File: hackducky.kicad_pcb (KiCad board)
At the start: 2 copper layers, 21 x 42.4 mm, 52 parts, among them J1 USB_A, J2 Conn_02x02_Top_Bottom, J3 Micro_SD_Card, P2 USB_C_Plug, SW3 BOOT_SEL, SW4 BOOT_SEL, U1 W25Q16JVSS, U2 AP2112K-3.3, U3 USBLC6-2P6, U4 RP2040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

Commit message: done beter
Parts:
- moved G*** 1.85 mm to (82.5, 86.6)
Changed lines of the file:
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@@
 	(footprint "LOGO"
 		(layer "F.Cu")
-		(at 82.5 84.75 90)
+		(at 82.45 86.6 90)
 		(property "Reference" "G***"
 			(at 0 0 90)
@@
 	)
 	(gr_text "Souptik.me & Aarav J."
-		(at 90.5 93 -90)
+		(at 93.68 92.44 -90)
 		(layer "F.SilkS")
 		(effects

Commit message: will do pr latr
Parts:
- R16, R17, R18, R19, R20, R21: moved to B.Cu
- moved G*** 3.71 mm to (91.9, 87.9)
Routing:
- net +3V3: track 103.6 -> 113.2 mm, vias 9 -> 12
- net GND: track 94.1 -> 101.2 mm
- net SD_CLK: track 21.2 -> 22.0 mm, vias 2 -> 3
- net SD_MOSI: track 21.8 -> 22.4 mm
- net SD_MISO: track 17.7 -> 17.4 mm, vias 0 -> 2
- net Net-(J3-DAT1): track 1.39 -> 1.26 mm, vias 0 -> 1
- net Net-(J3-DAT2): track 1.59 -> 1.66 mm, vias 0 -> 1
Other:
- board text added: "Souptik & Aarav."
- board text removed: "Souptik.me & Aarav J."

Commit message: fixed silkscreen
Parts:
- removed the G*** at (133.2, 55.2)
- removed the G*** at (60.2, 85.0)
- moved G*** 0.32 mm to (92.0, 88.2)
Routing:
- net +3V3: track 113.2 -> 126.0 mm, vias 12 -> 17
- net GND: track 101.2 -> 95.7 mm, vias 30 -> 31
- net SD_CS: track 21.9 -> 22.7 mm, vias 2 -> 3
- net SD_MISO: track 17.4 -> 17.8 mm, vias 2 -> 1

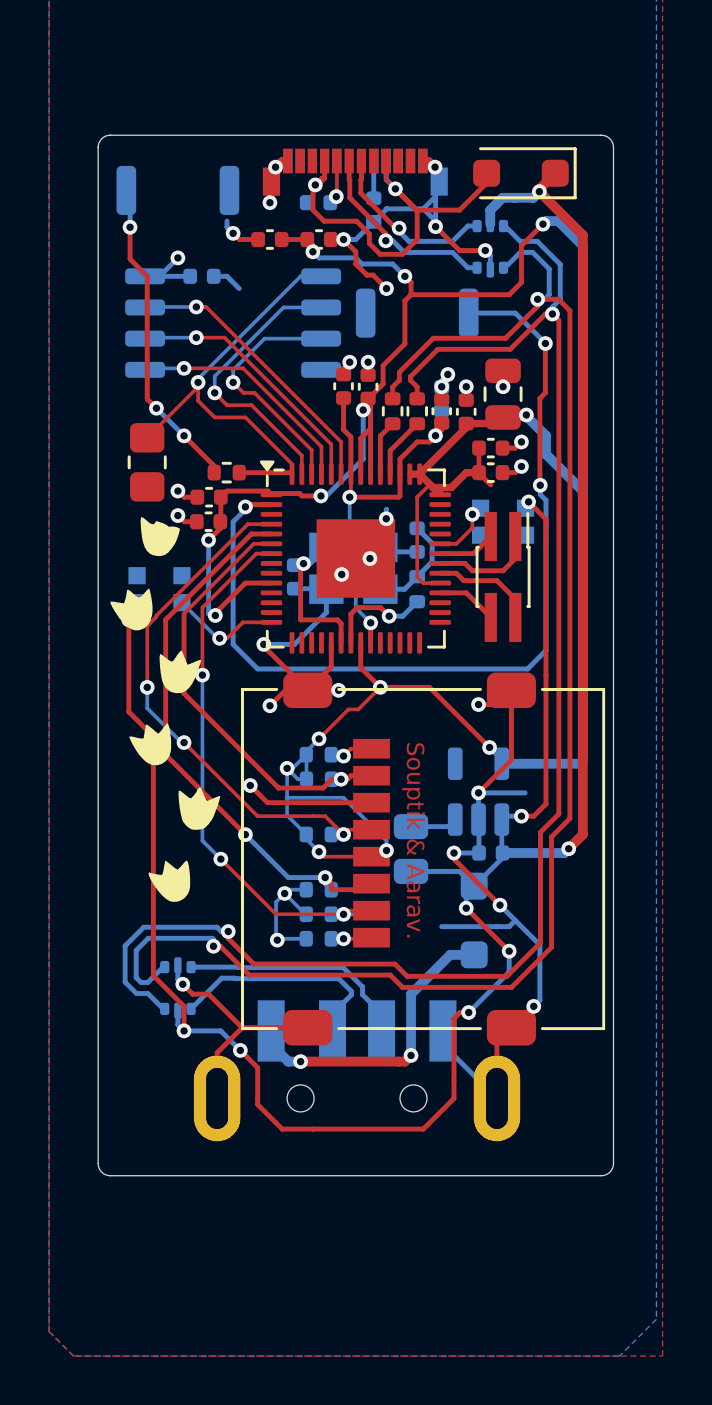
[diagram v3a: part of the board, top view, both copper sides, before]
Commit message: v4 mostly tuned paths
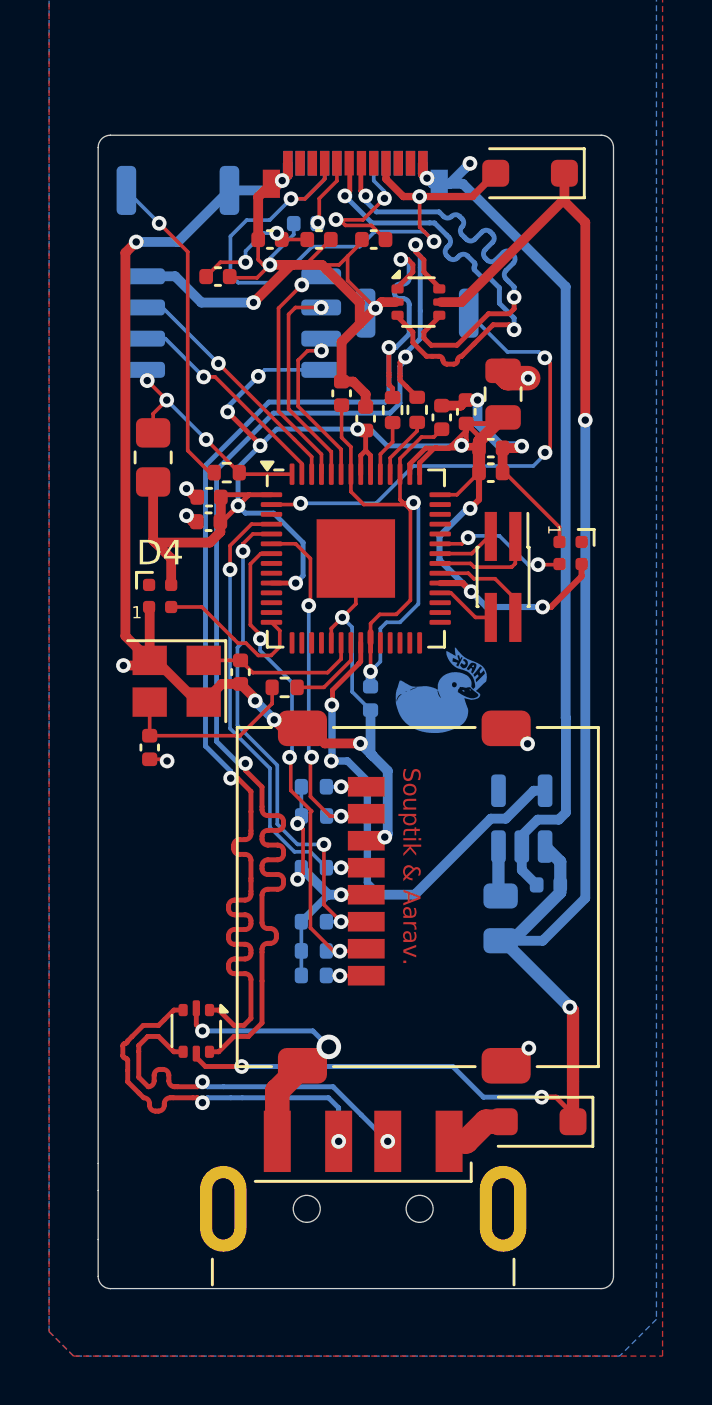
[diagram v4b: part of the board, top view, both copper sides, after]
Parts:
- removed the G*** at (82.5, 86.6)
- removed the G*** at (92.0, 88.2)
- added G*** (x2): LOGO, LOGO, B.Cu at (93.5, 86.3)
- C12, C13, C16, D3, J1, R5, R9, U3, U5, Y1: moved to F.Cu
- D1, D4: footprint LED_SMD:LED_WS2812B-2020_PLCC4_2.0x2.0mm -> LED_SMD:LED_SK6812_EC15_1.5x1.5mm; moved to F.Cu
- G***: moved to B.Cu
- moved C12 13.8 mm to (81.6, 88.5)
- moved C8 12.5 mm to (90.6, 86.5), turned to -90 degrees
- moved D3 8.61 mm to (97.5, 103.7), turned to 180 degrees
- moved Y1 8.54 mm to (82.7, 85.8), turned to 180 degrees
- moved R9 6.72 mm to (87.1, 86.0), turned to 180 degrees
- moved R6 4.62 mm to (95.9, 95.4)
- moved J1 4.51 mm to (90.3, 114.2)
- moved C13 4.46 mm to (85.3, 85.4)
- moved U5 3.69 mm to (92.5, 70.3), turned to 0 degrees
- moved D1 3.03 mm to (98.8, 80.5), turned to -90 degrees
- moved C14 2.69 mm to (97.8, 94.0)
- moved U2 2.08 mm to (96.8, 91.3)
- moved U3 1.90 mm to (83.5, 100.0)
- moved J3 1.56 mm to (92.5, 94.5)
- moved R20 1.51 mm to (88.3, 91.2)
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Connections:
- D1 pad 3: +5V -> +3V3
- D4 pad 3: +5V -> +3V3
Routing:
- net GND: track 95.7 -> 154.9 mm, vias 31 -> 23
- net +5V: track 99.6 -> 72.3 mm, vias 10 -> 4
- net +3V3: track 126.0 -> 108.0 mm
- net GPIO0: track 36.6 -> 20.0 mm
- net DUPC-: track 7.22 -> 18.8 mm, vias 1 -> 2
- net D+: track 61.4 -> 50.4 mm, vias 2 -> 3
- net D-: track 61.4 -> 50.4 mm, vias 2 -> 3
- net DUPC+: track 8.04 -> 18.9 mm, vias 1 -> 2
- net +1V1: track 17.6 -> 28.0 mm, vias 3 -> 2
- net Net-(D2-A): track 19.3 -> 29.3 mm, vias 2 -> 3
- net Net-(D3-A): track 12.4 -> 2.58 mm, vias 2 -> 0
- net QSPI_SS: track 18.2 -> 9.80 mm, vias 1 -> 3
- net DUPA-: track 9.21 -> 15.9 mm, vias 0 -> 2
- net DUPA+: track 9.44 -> 15.9 mm, vias 0 -> 2
- net Net-(P2-VCONN): track 1.52 -> 6.31 mm, vias 0 -> 2
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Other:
- board size 21 x 42.4 mm -> 21 x 47 mm
